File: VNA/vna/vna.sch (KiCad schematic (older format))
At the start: 6 parts, among them J1 USB_B_Micro, J2 DC_IN_Conn, J3 Pt1, J4 Pt2, U1 74HCT04

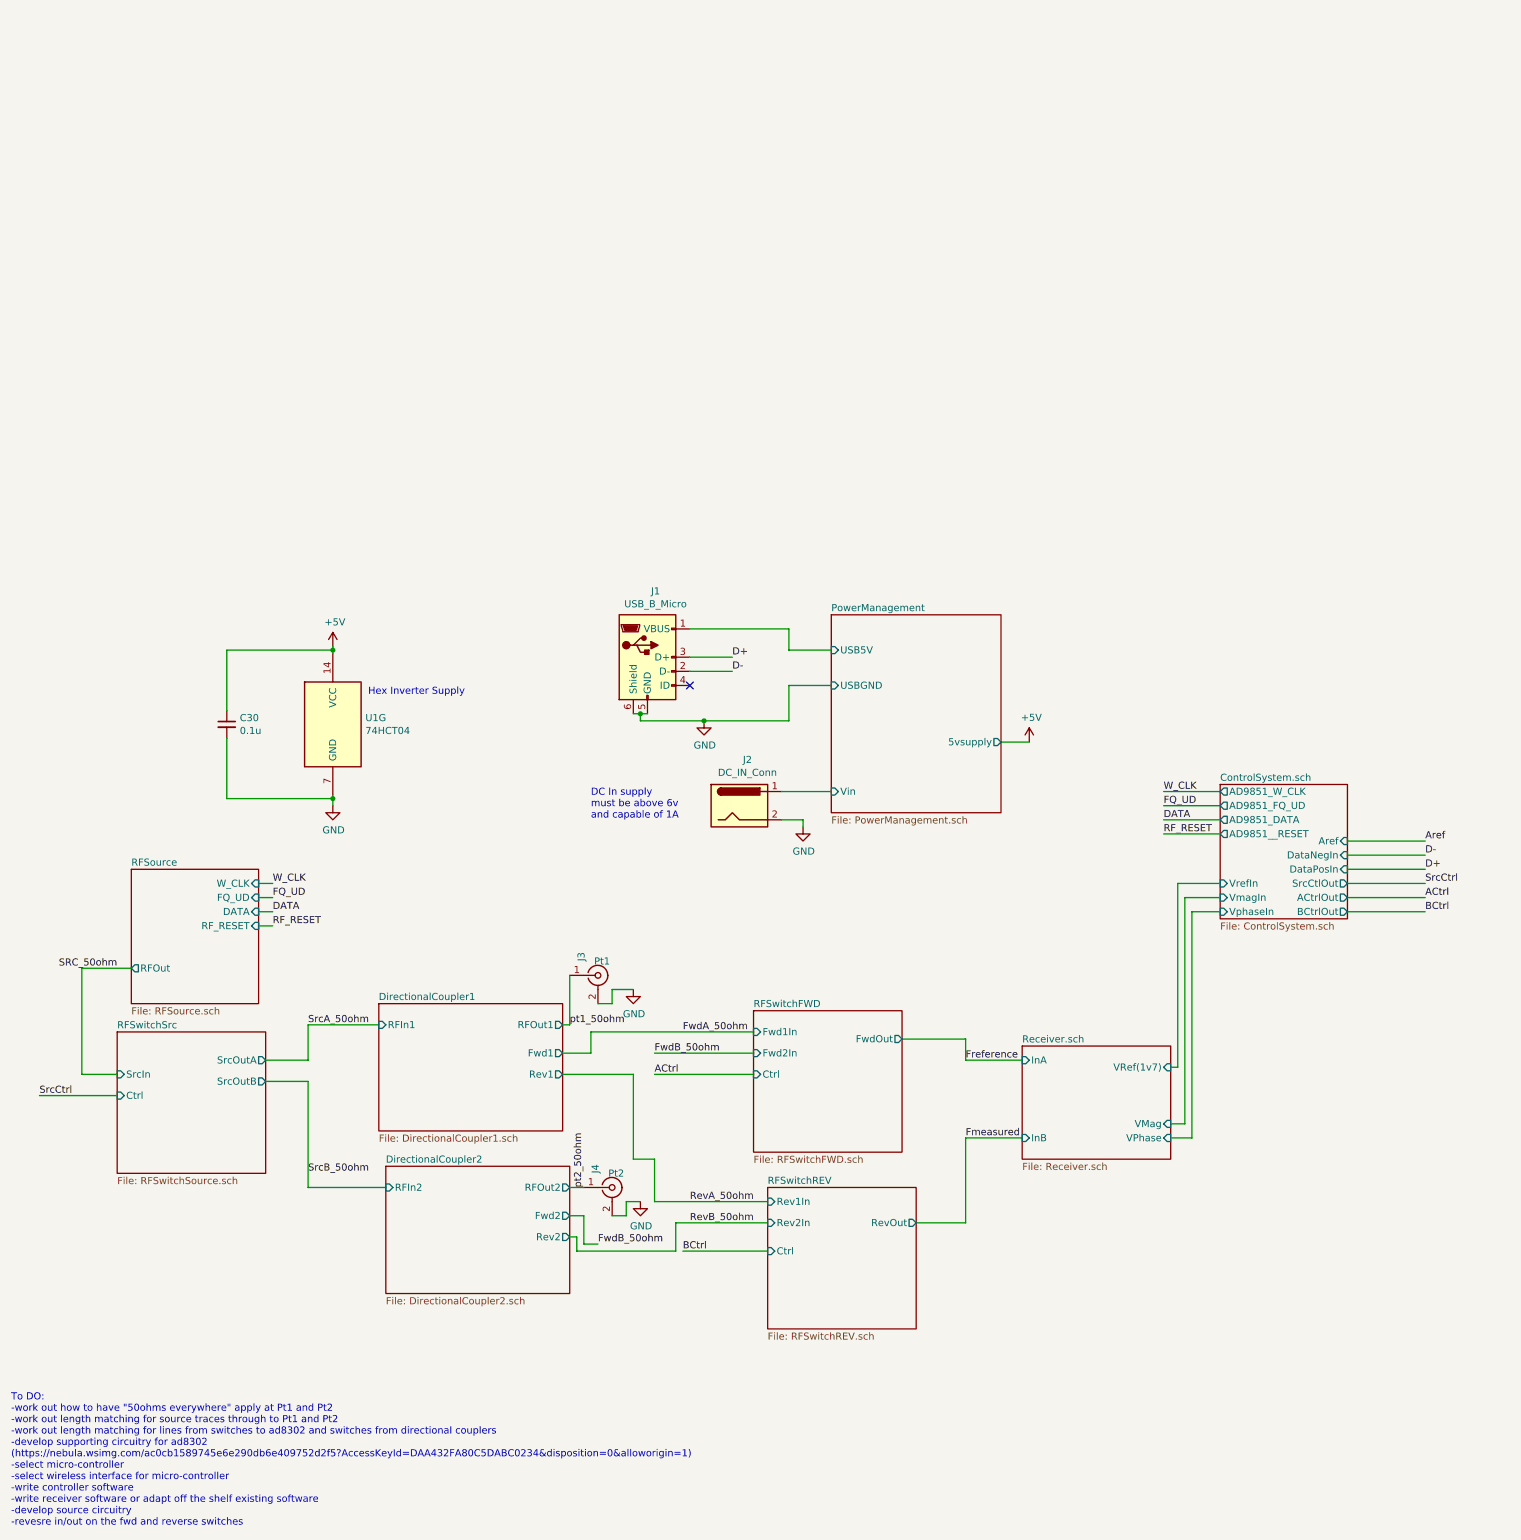
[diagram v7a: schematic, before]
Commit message: initial pcb design
initial layout and grouping of components complete
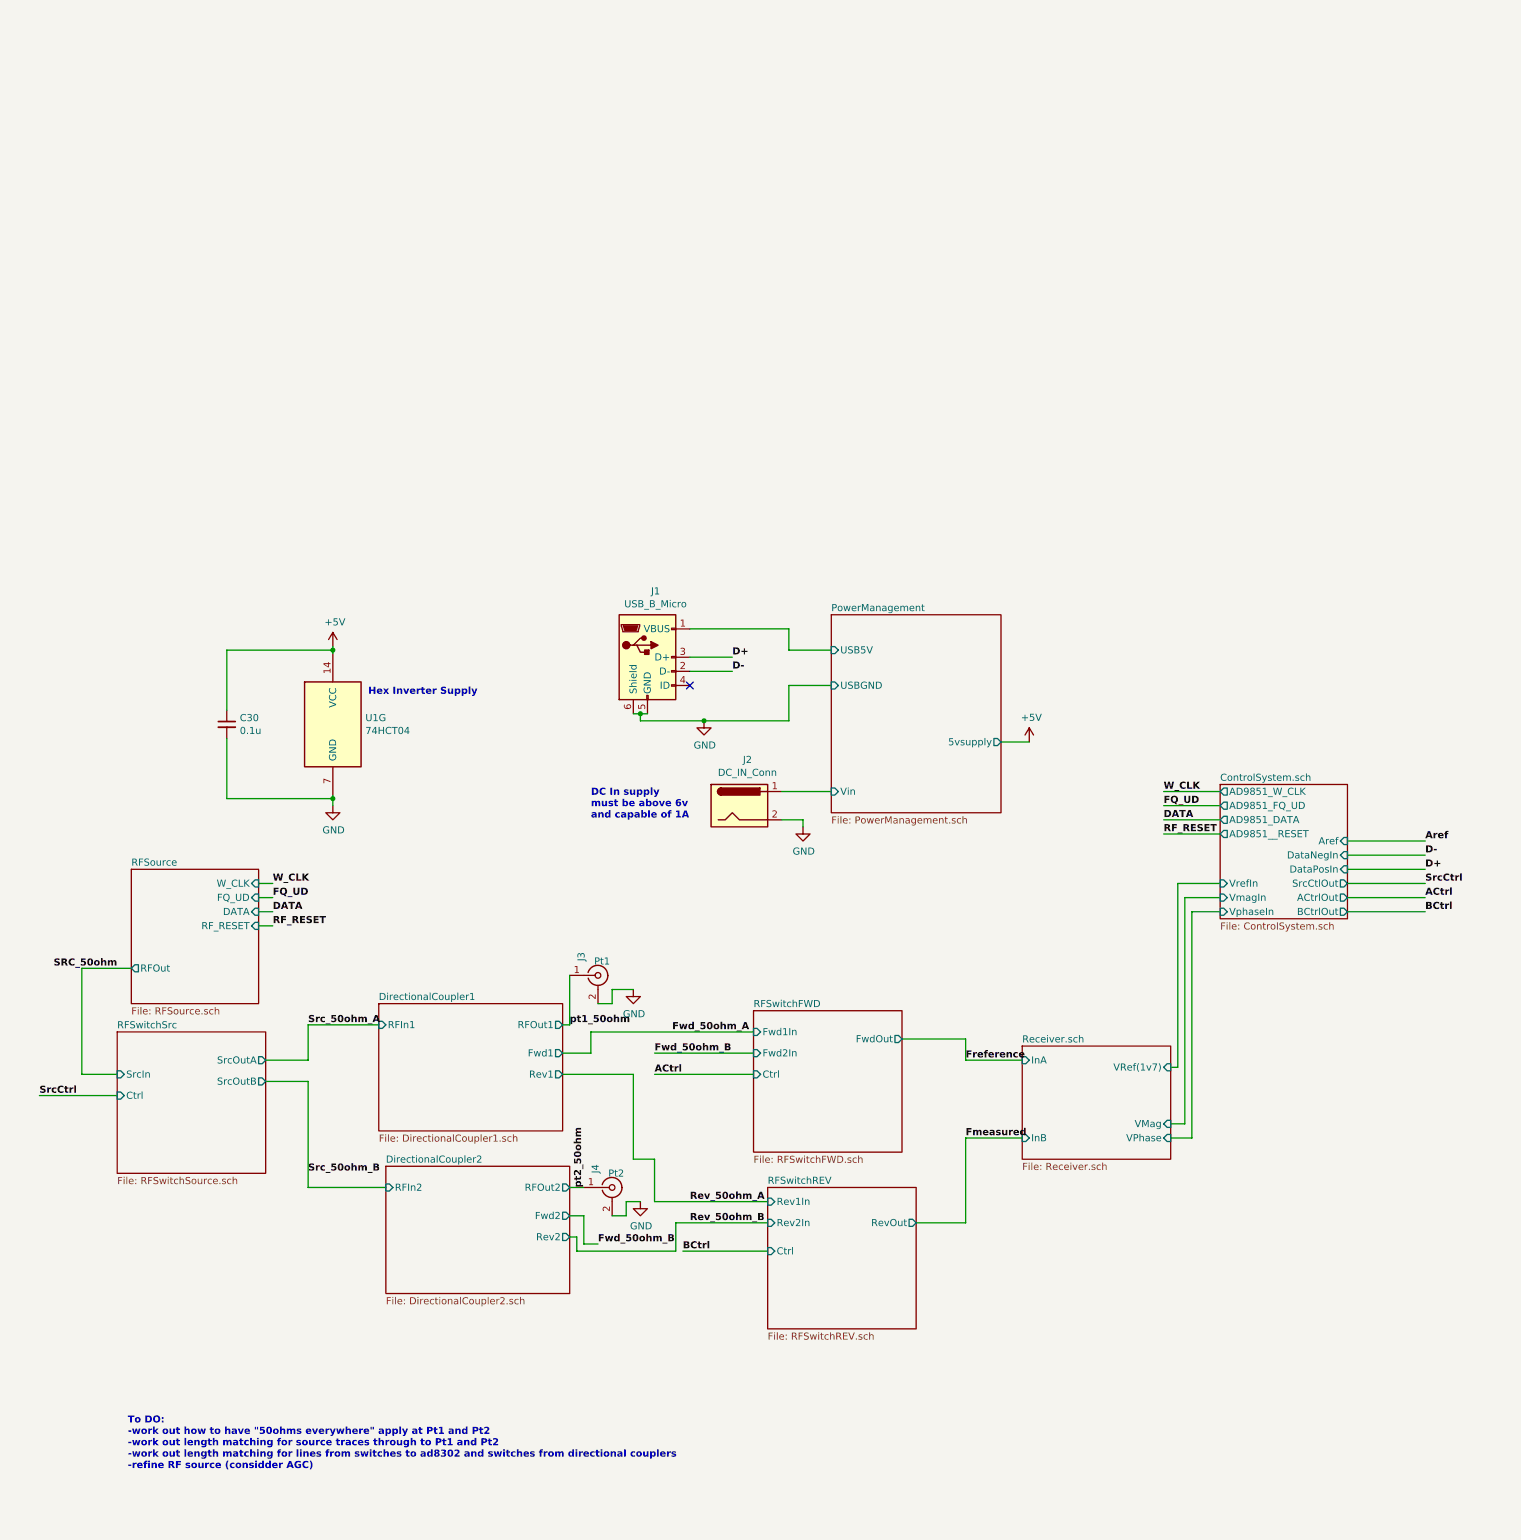
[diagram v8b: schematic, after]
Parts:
- C30: footprint Capacitor_SMD:C_1206_3216Metric_Pad1.42x1.75mm_HandSolder -> Capacitor_SMD:C_0805_2012Metric_Pad1.15x1.40mm_HandSolder
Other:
- note added: "To DO:\n-work out how to have "50ohms everywhere" apply at Pt1 and Pt2\n-work out length matching for source traces through to Pt1 and Pt2\n-work out length matching for lines from switches to ad8302 and switches from directional couplers\n-refine RF source (considder AGC)"
- note removed: "To DO:\n-work out how to have "50ohms everywhere" apply at Pt1 and Pt2\n-work out length matching for source traces through to Pt1 and Pt2\n-work out length matching for lines from switches to ad8302 and switches from directional couplers\n-develop supporting circuitry for ad8302 \n(https://nebula.wsimg.com/ac0cb1589745e6e290db6e409752d2f5?AccessKeyId=DAA432FA80C5DABC0234&disposition=0&alloworigi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"
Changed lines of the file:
@@
 Comment4 ""
 $EndDescr
-Text Notes 700  7550 0    50   ~ 0
-To DO:\n-work out how to have "50ohms everywhere" apply at Pt1 and Pt2\n-work out length matching for source traces through to Pt1 and Pt2\n-work out length matching for lines from switches to ad8302 and switches from directional couplers\n-develop supporting circuitry for ad8302 \n(https://nebula.wsimg.com/ac0cb1589745e6e290db6e409752d2f5?AccessKeyId=DAA432FA80C5DABC0234&disposition=0&alloworigin=1)\n-select micro-controller\n-select wireless interface for micro-controller\n-write controller software\n-write receiver software or adapt off the shelf existing software\n-develop source circuitry\n-revesre in/out on the fwd and reverse switches
+Text Notes 1525 7150 0    50   ~ 10
+To DO:\n-work out how to have "50ohms everywhere" apply at Pt1 and Pt2\n-work out length matching for source traces through to Pt1 and Pt2\n-work out length matching for lines from switches to ad8302 and switches from directional couplers\n-refine RF source (considder AGC)
 $Comp
 L Connector:Conn_Coaxial J3
@@
 F5 "Rev2In" I L 6050 5400 50
 $EndSheet
-Text Label 2800 5050 0    50   ~ 0
-SrcB_50ohm
-Text Label 2800 4000 0    50   ~ 0
-SrcA_50ohm
+Text Label 2800 5050 0    50   ~ 10
+Src_50ohm_B
+Text Label 2800 4000 0    50   ~ 10
+Src_50ohm_A
 Wire Wire Line
 	4700 5600 5400 5600
@@
 Wire Wire Line
 	5050 5250 5150 5250
-Text Label 5450 4050 0    50   ~ 0
-FwdA_50ohm
-Text Label 5250 4200 0    50   ~ 0
-FwdB_50ohm
-Text Label 5500 5250 0    50   ~ 0
-RevA_50ohm
-Text Label 5500 5400 0    50   ~ 0
-RevB_50ohm
+Text Label 5375 4050 0    50   ~ 10
+Fwd_50ohm_A
+Text Label 5250 4200 0    50   ~ 10
+Fwd_50ohm_B
+Text Label 5500 5250 0    50   ~ 10
+Rev_50ohm_A
+Text Label 5500 5400 0    50   ~ 10
+Rev_50ohm_B
 $Sheet
 S 7850 4150 1050 800
@@
 	1    0    0    -1
 $EndComp
-Text Label 4850 5550 0    50   ~ 0
-FwdB_50ohm
-Text Label 7450 4800 0    50   ~ 0
+Text Label 4850 5550 0    50   ~ 10
+Fwd_50ohm_B
+Text Label 7450 4800 0    50   ~ 10
 Fmeasured
-Text Label 7450 4250 0    50   ~ 0
+Text Label 7450 4250 0    50   ~ 10
 Freference
 Wire Wire Line
@@
 Wire Wire Line
 	1450 4500 900  4500
-Text Label 900  4500 0    50   ~ 0
+Text Label 900  4500 0    50   ~ 10
 SrcCtrl
-Text Label 5250 4350 0    50   ~ 0
+Text Label 5250 4350 0    50   ~ 10
 ACtrl
-Text Label 5450 5600 0    50   ~ 0
+Text Label 5450 5600 0    50   ~ 10
 BCtrl
 $Sheet
@@
 Wire Wire Line
 	8900 4800 9050 4800
-Text Label 10700 2800 0    50   ~ 0
+Text Label 10700 2800 0    50   ~ 10
 D-
-Text Label 10700 2900 0    50   ~ 0
+Text Label 10700 2900 0    50   ~ 10
 D+
 NoConn ~ 5500 1600
@@
 Wire Wire Line
 	5500 1500 5800 1500
-Text Label 5800 1400 0    50   ~ 0
+Text Label 5800 1400 0    50   ~ 10
 D+
-Text Label 5800 1500 0    50   ~ 0
+Text Label 5800 1500 0    50   ~ 10
 D-
 Wire Wire Line
@@
 Wire Wire Line
 	10150 3200 10700 3200
-Text Label 10700 3000 0    50   ~ 0
+Text Label 10700 3000 0    50   ~ 10
 SrcCtrl
-Text Label 10700 3100 0    50   ~ 0
+Text Label 10700 3100 0    50   ~ 10
 ACtrl
-Text Label 10700 3200 0    50   ~ 0
+Text Label 10700 3200 0    50   ~ 10
 BCtrl
 Wire Wire Line
@@
 	1    0    0    -1
 $EndComp
-Text Label 4750 5150 1    50   ~ 0
+Text Label 4750 5150 1    50   ~ 10
 pt2_50ohm
-Text Label 4650 4000 0    50   ~ 0
+Text Label 4650 4000 0    50   ~ 10
 pt1_50ohm
 Wire Wire Line
@@
 Wire Wire Line
 	4750 5550 4850 5550
-Text Label 1450 3600 2    50   ~ 0
+Text Label 1450 3600 2    50   ~ 10
 SRC_50ohm
 $Comp
@@
 Wire Wire Line
 	6300 2550 6300 2600
-Text Notes 4800 2550 0    50   ~ 0
+Text Notes 4800 2550 0    50   ~ 10
 DC In supply \nmust be above 6v\nand capable of 1A
-Text Notes 3225 1675 0    50   ~ 0
+Text Notes 3225 1675 0    50   ~ 10
 Hex Inverter Supply
 Wire Wire Line
@@
 Wire Wire Line
 	10150 2700 10700 2700
-Text Label 10700 2700 0    50   ~ 0
+Text Label 10700 2700 0    50   ~ 10
 Aref
 Wire Wire Line
@@
 Wire Wire Line
 	9250 2650 8850 2650
-Text Label 8850 2350 0    50   ~ 0
+Text Label 8850 2350 0    50   ~ 10
 W_CLK
-Text Label 8850 2450 0    50   ~ 0
+Text Label 8850 2450 0    50   ~ 10
 FQ_UD
-Text Label 8850 2550 0    50   ~ 0
+Text Label 8850 2550 0    50   ~ 10
 DATA
-Text Label 8850 2650 0    50   ~ 0
+Text Label 8850 2650 0    50   ~ 10
 RF_RESET
-Text Label 2550 3000 0    50   ~ 0
+Text Label 2550 3000 0    50   ~ 10
 W_CLK
-Text Label 2550 3100 0    50   ~ 0
+Text Label 2550 3100 0    50   ~ 10
 FQ_UD
-Text Label 2550 3200 0    50   ~ 0
+Text Label 2550 3200 0    50   ~ 10
 DATA
-Text Label 2550 3300 0    50   ~ 0
+Text Label 2550 3300 0    50   ~ 10
 RF_RESET
 Wire Wire Line
@@
 F 0 "C30" H 2317 1921 50  0000 L CNN
 F 1 "0.1u" H 2317 1830 50  0000 L CNN
-F 2 "Capacitor_SMD:C_1206_3216Metric_Pad1.42x1.75mm_HandSolder" H 2225 1875 50  0001 C CNN
+F 2 "Capacitor_SMD:C_0805_2012Metric_Pad1.15x1.40mm_HandSolder" H 2225 1875 50  0001 C CNN
 F 3 "~" H 2225 1875 50  0001 C CNN
 	1    2225 1875
